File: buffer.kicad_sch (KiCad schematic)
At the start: 35 parts, among them U1501 OPA1662AIDGKRQ1, U1502 OPA2387

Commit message: replace passives with 0402
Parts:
- C1504, C1505, C1506: footprint Capacitor_SMD:C_0603_1608Metric_Pad1.08x0.95mm_HandSolder -> Capacitor_SMD:C_0402_1005Metric; MPN C0603C105K8RACTU -> C0402C105K9PACTU
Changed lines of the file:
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@@
       (effects (font (size 1.27 1.27)) (justify left))
     )
-    (property "Footprint" "Capacitor_SMD:C_0603_1608Metric_Pad1.08x0.95mm_HandSolder" (at 152.4 77.47 0)
+    (property "Footprint" "Capacitor_SMD:C_0402_1005Metric" (at 152.4 77.47 0)
       (effects (font (size 1.27 1.27)) hide)
     )
@@
       (effects (font (size 1.27 1.27)) hide)
     )
-    (property "MPN" "C0603C105K8RACTU" (at 152.4 77.47 0)
+    (property "MPN" "C0402C105K9PACTU" (at 152.4 77.47 0)
       (effects (font (size 1.27 1.27)) hide)
     )
@@
       (effects (font (size 1.27 1.27)) (justify left))
     )
-    (property "Footprint" "Capacitor_SMD:C_0603_1608Metric_Pad1.08x0.95mm_HandSolder" (at 150.495 42.545 0)
+    (property "Footprint" "Capacitor_SMD:C_0402_1005Metric" (at 150.495 42.545 0)
       (effects (font (size 1.27 1.27)) hide)
     )
@@
       (effects (font (size 1.27 1.27)) hide)
     )
-    (property "MPN" "C0603C105K8RACTU" (at 150.495 42.545 0)
+    (property "MPN" "C0402C105K9PACTU" (at 150.495 42.545 0)
       (effects (font (size 1.27 1.27)) hide)
     )
@@
       (effects (font (size 1.27 1.27)))
     )
-    (property "Footprint" "Capacitor_SMD:C_0603_1608Metric_Pad1.08x0.95mm_HandSolder" (at 207.645 67.31 0)
+    (property "Footprint" "Capacitor_SMD:C_0402_1005Metric" (at 207.645 67.31 0)
       (effects (font (size 1.27 1.27)) hide)
     )
@@
       (effects (font (size 1.27 1.27)) hide)
     )
-    (property "MPN" "C0603C105K8RACTU" (at 207.645 67.31 0)
-      (effects (font (size 1.27 1.27)) hide)
-    )
+    (property "MPN" "C0402C105K9PACTU" (at 207.645 67.31 0)
+      (effects (font (size 1.27 1.27)) hide)
+    )

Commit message: (sch) add tantulum cap
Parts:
- added C1608: 100uF, Capacitor_Tantalum_SMD:CP_EIA-1608-10_AVX-L, symbol Device:C_Small
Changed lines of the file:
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@@
+    )
+  )
+  (symbol (lib_id "Device:C_Small") (at 37.465 149.86 0) (unit 1)
+    (in_bom yes) (on_board yes) (dnp no)
+    (property "Reference" "C1608" (at 40.64 149.2313 0)
+      (effects (font (size 1.27 1.27)) (justify left))
+    )
+    (property "Value" "100uF" (at 40.64 151.7713 0)
+      (effects (font (size 1.27 1.27)) (justify left))
+    )
+    (property "Footprint" "Capacitor_Tantalum_SMD:CP_EIA-1608-10_AVX-L" (at 37.465 149.86 0)
+      (effects (font (size 1.27 1.27)) hide)
+    )
+    (property "Datasheet" "~" (at 37.465 149.86 0)
+      (effects (font (size 1.27 1.27)) hide)
+    )
+    (property "MPN" "F980G107MMAAH1" (at 37.465 149.86 0)
+      (effects (font (size 1.27 1.27)) hide)
+    )
+    (property "Mfr." "KYOCERA AVX" (at 37.465 149.86 0)
+      (effects (font (size 1.27 1.27)) hide)
+    )
+    (property "Note" "Tantalum" (at 45.085 153.67 0)
+      (effects (font (size 1.27 1.27)))
+    )
+    (pin "1")
+    (pin "2")
+    (instances
+      (project "kleinvoet"
+        (path "/4185c36c-c66e-4dbd-be5d-841e551f4885/b53619ea-788f-4bc9-9946-594014d7d22c/00000000-0000-0000-0000-00005f9c4001"
+          (reference "C1608") (unit 1)
+        )
+      )
     )
   )

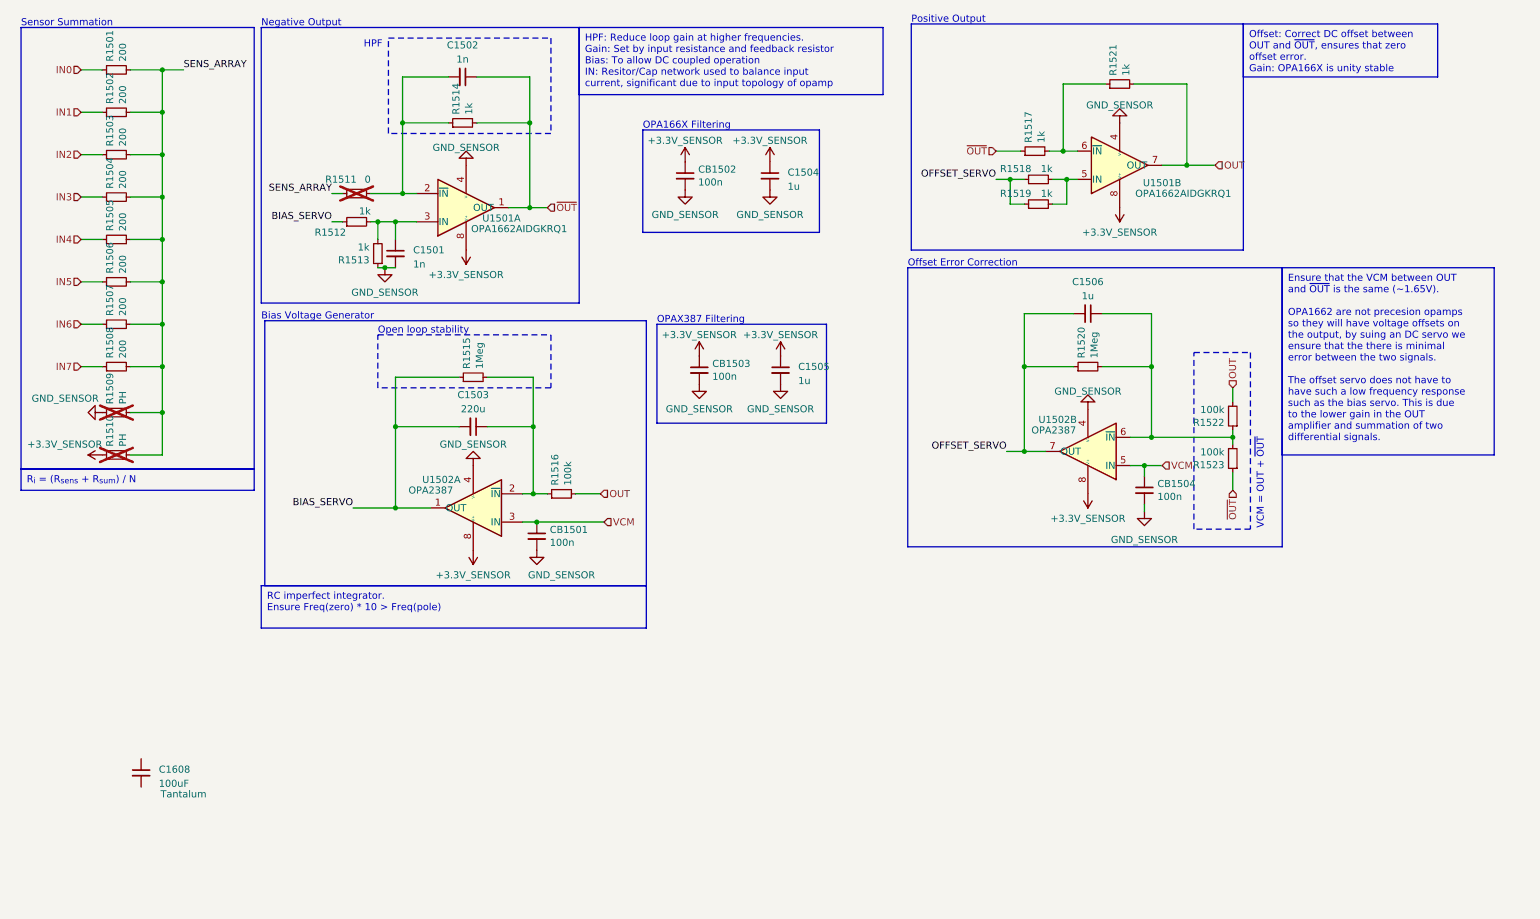
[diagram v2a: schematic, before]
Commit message: (sch) change summing stage to recommend - remove servo
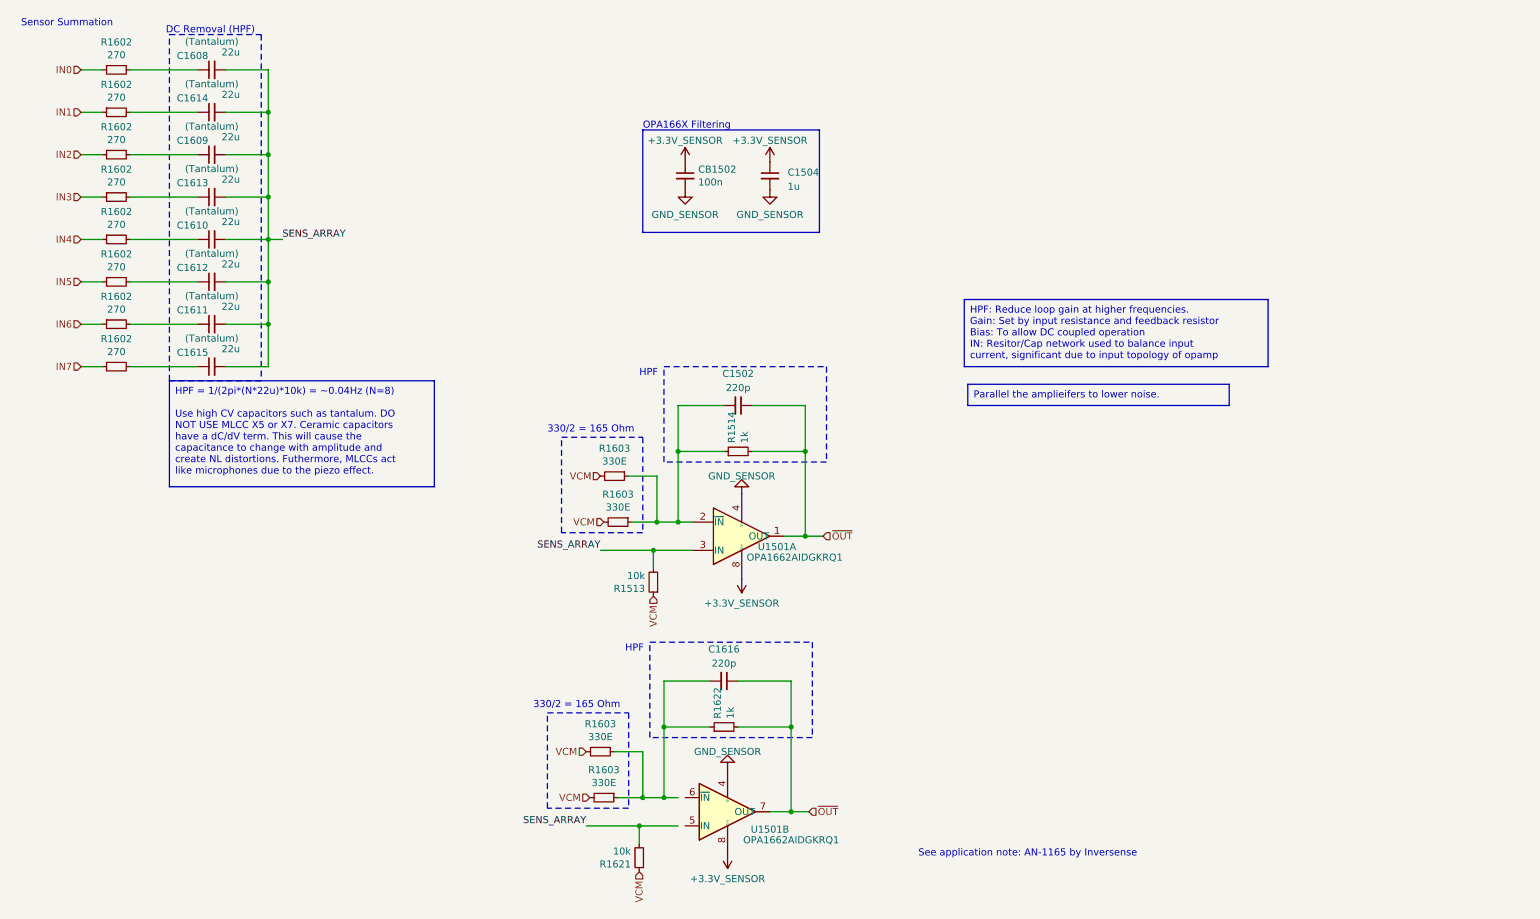
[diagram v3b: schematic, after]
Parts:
- removed C1501: 1n, Capacitor_SMD:C_0402_1005Metric, symbol Device:C_Small
- removed C1503: 220u, Capacitor_SMD:C_1206_3216Metric, symbol Device:C_Small
- removed C1505, C1506: 1u, Capacitor_SMD:C_0402_1005Metric, symbol Device:C_Small
- removed CB1501, CB1503, CB1504: 100n, Capacitor_SMD:C_0402_1005Metric, symbol Device:C_Small
- removed R1501, R1502, R1503, R1504, R1505, R1506, R1507, R1508: 200, Resistor_SMD:R_0603_1608Metric_Pad0.98x0.95mm_HandSolder, symbol Device:R_Small
- removed R1509, R1510: PH, Resistor_SMD:R_0603_1608Metric_Pad0.98x0.95mm_HandSolder, symbol Device:R_Small
- removed R1511: 0, Resistor_SMD:R_0603_1608Metric_Pad0.98x0.95mm_HandSolder, symbol Device:R_Small
- removed R1512, R1517, R1518, R1519, R1521: 1k, Resistor_SMD:R_0402_1005Metric, symbol Device:R_Small
- removed R1515, R1520: 1Meg, Resistor_SMD:R_0603_1608Metric_Pad0.98x0.95mm_HandSolder, symbol Device:R_Small
- removed R1516, R1522, R1523: 100k, Resistor_SMD:R_0402_1005Metric, symbol Device:R_Small
- removed U1502: OPA2387, grootvoet:OPA1662AIDGK, symbol grootvoet:OPA2387
- added C1609, C1610, C1611, C1612, C1613, C1614, C1615: 22u, Capacitor_Tantalum_SMD:CP_EIA-1608-10_AVX-L, symbol Device:C_Small
- added C1616: 220p, Capacitor_SMD:C_0402_1005Metric, symbol Device:C_Small
- added R1602 (x8): 270, Resistor_SMD:R_0402_1005Metric, symbol Device:R_Small
- added R1603 (x4): 330E, Resistor_SMD:R_0402_1005Metric, symbol Device:R_Small
- added R1621: 10k, Resistor_SMD:R_0402_1005Metric, symbol Device:R_Small
- added R1622: 1k, Resistor_SMD:R_0402_1005Metric, symbol Device:R_Small
- C1502: value 1n -> 220p
- C1608: value 100uF -> 22u; MPN F980G107MMAAH1 -> (none); Note Tantalum -> (Tantalum)
- R1513: value 1k -> 10k; MPN RT0402FRE071KL -> (none)
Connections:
- net OUT is gone; now on net ~{OUT}: U1501.7 (OUT)
- net GND: no longer R1513.1
- net IN0: now also R1602.1
- net IN1: now also R1602.1
- net IN2: now also R1602.1
- net IN3: now also R1602.1
- net IN4: now also R1602.1
- net IN5: now also R1602.1
- net IN6: now also R1602.1
- net IN7: now also R1602.1
- net SENS_ARRAY: now also C1608.2, R1513.2, U1501.3 (IN), C1609.2, C1610.2, C1611.2, C1612.2, C1613.2, C1614.2, C1615.2, R1621.2
- net VCM: now also R1513.1, R1603.2, R1603.2, R1603.2, R1603.2, R1621.1
- net ~{OUT}: now also C1616.1, R1622.2
- net at C1502.2, R1514.1, U1501.2 (~{IN}): now also R1603.1, R1603.1
- net at C1608.1: now also R1602.2
- new net: C1612.1, R1602.2
- new net: C1610.1, R1602.2
- new net: C1609.1, R1602.2
- new net: C1616.2, R1603.1, R1603.1, R1622.1
- new net: C1611.1, R1602.2
- new net: C1615.1, R1602.2
- new net: C1614.1, R1602.2
- new net: C1613.1, R1602.2
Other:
- note added: "330/2 = 165 Ohm"
- note added: "DC Removal (HPF)"
- note added: "See application note: AN-1165 by Inversense"
- note removed: "Bias Voltage Generator"
- note removed: "Negative Output"
- note removed: "OPAX387 Filtering"
- note removed: "Offset Error Correction"
- note removed: "Open loop stability"
- note removed: "Positive Output"
- note removed: "VCM = OUT + ~{OUT}"
- moved on the sheet: C1502, C1608, R1513, R1514, U1501A, U1501B

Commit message: (sch) annotate preamp
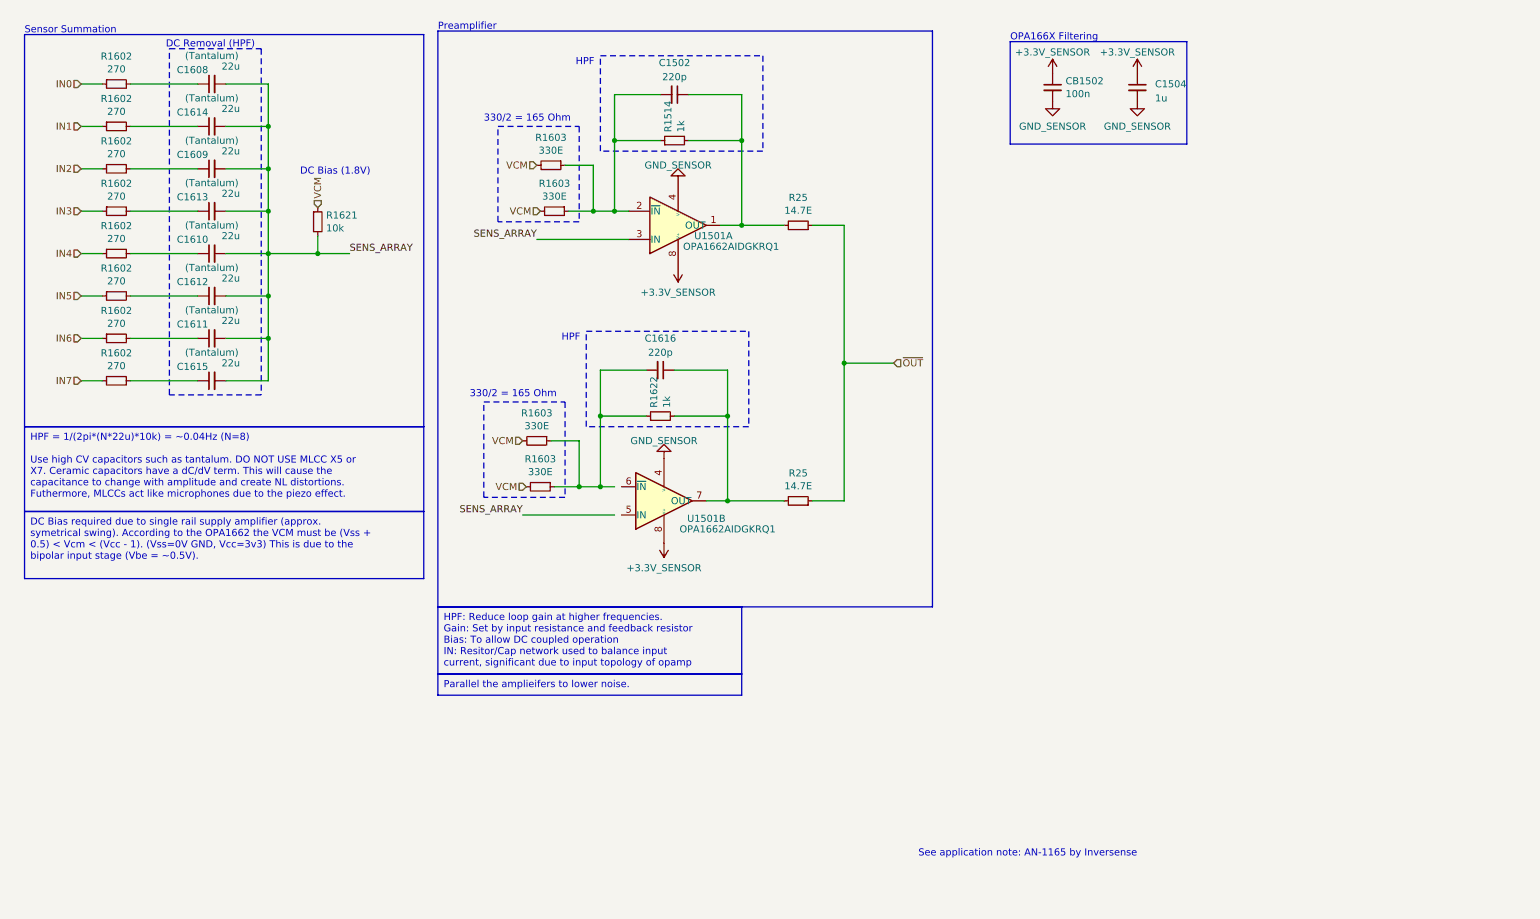
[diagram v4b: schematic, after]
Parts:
- removed R1513: 10k, Resistor_SMD:R_0402_1005Metric, symbol Device:R_Small
- added R25 (x2): 14.7E, Resistor_SMD:R_0402_1005Metric, symbol Device:R_Small
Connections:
- net ~{OUT}: now also R25.1, R25.1; no longer C1502.1, C1616.1, R1514.2, R1622.2, U1501.1 (OUT), U1501.7 (OUT)
- new net: C1502.1, R1514.2, R25.2, U1501.1 (OUT)
- new net: C1616.1, R1622.2, R25.2, U1501.7 (OUT)
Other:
- note added: "DC Bias (1.8V)"
- note added: "Preamplifier"
- moved on the sheet: C1502, C1504, C1608, C1609, C1610, C1611, C1612, C1613, C1614, C1615, C1616, CB1502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

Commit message: (sch) rough layout sensorboard
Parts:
- removed R1602 (x8): 270, Resistor_SMD:R_0402_1005Metric, symbol Device:R_Small
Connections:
- net IN0: now also C1608.1
- net IN1: now also C1614.1
- net IN2: now also C1609.1
- net IN3: now also C1613.1
- net IN4: now also C1610.1
- net IN5: now also C1612.1
- net IN6: now also C1611.1
- net IN7: now also C1615.1
- net SENS_ARRAY: now also U1501.5 (IN)
- net PREAMP_A_FB: now reaches C1502.2, R1514.1, R1603.1, R1603.1, U1501.2 (~{IN})
- net PREAMP_A_OUT: now reaches C1502.1, R1514.2, R25.2, U1501.1 (OUT)
- net PREAMP_B_FB: now reaches C1616.2, R1603.1, R1603.1, R1622.1
- net PREAMP_B_FB: now also U1501.6 (~{IN})
- net PREAMP_B_OUT: now reaches C1616.1, R1622.2, R25.2, U1501.7 (OUT)
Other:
- moved on the sheet: C1608, C1609, C1610, C1611, C1612, C1613, C1614, C1615, R1621
